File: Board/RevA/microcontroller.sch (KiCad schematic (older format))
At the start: 3 parts

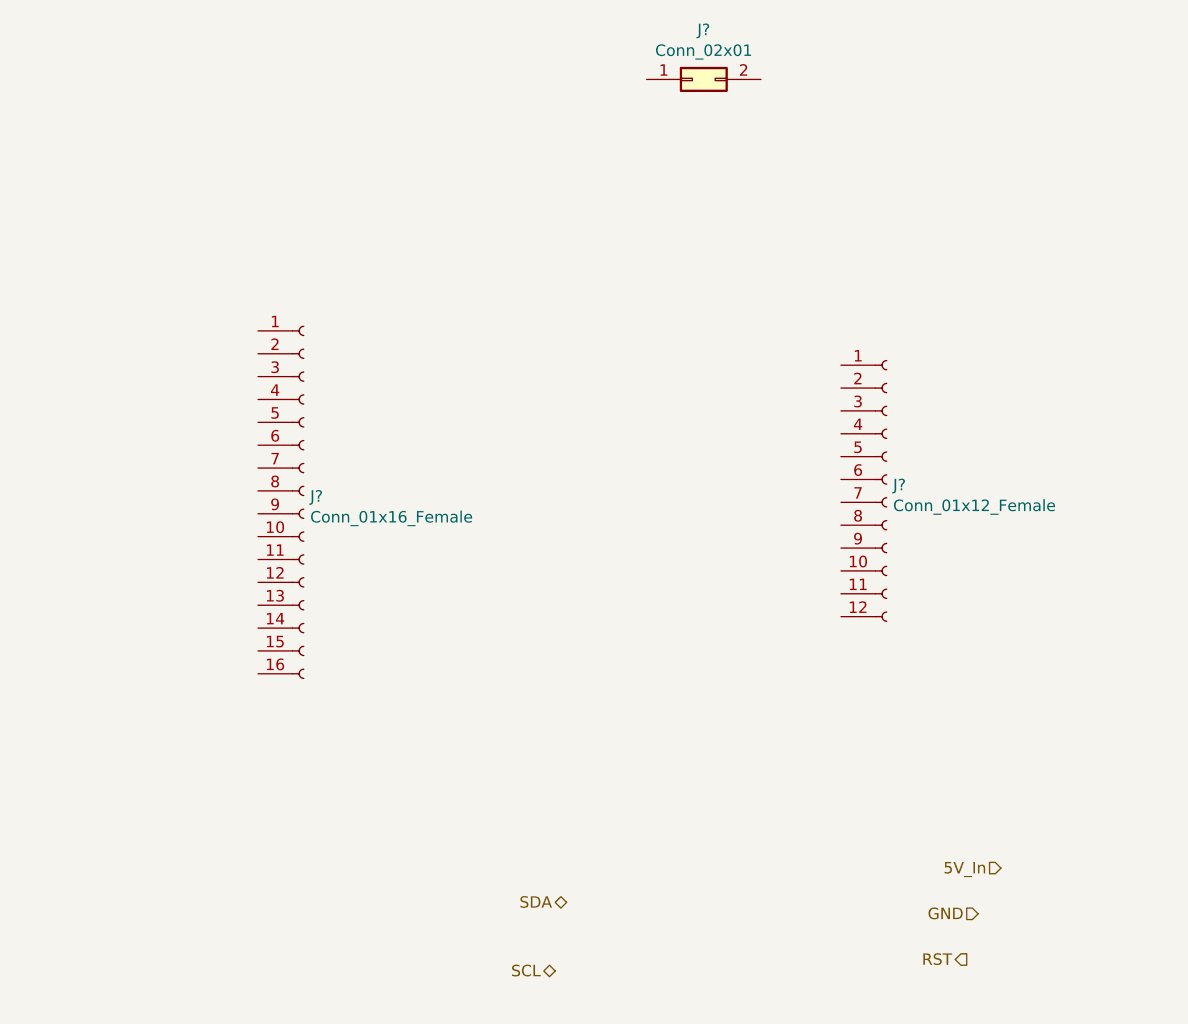
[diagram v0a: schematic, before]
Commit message: Added Microcontroller Logic to RevA
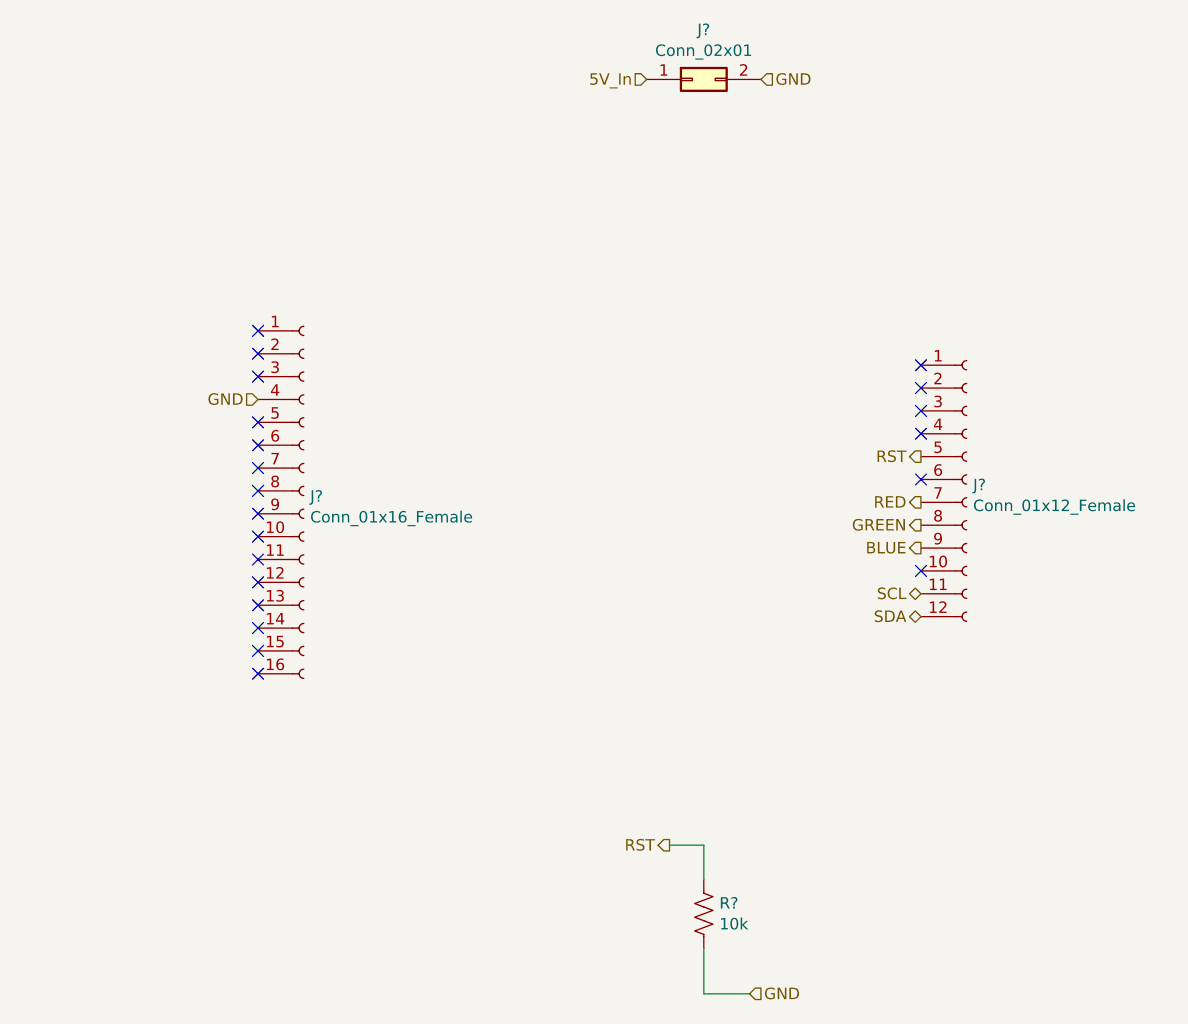
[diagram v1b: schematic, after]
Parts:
- added R?: 10k, symbol Device:R_US
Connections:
- net 5V_In: now also J?.1 (Pin_1)
- net GND: now also J?.2 (Pin_2), J?.4 (Pin_4), R?.2
- net RST: now also J?.5 (Pin_5), R?.1
- net SCL: now also J?.11 (Pin_11)
- net SDA: now also J?.12 (Pin_12)
- net RED: now reaches J?.7 (Pin_7)
- net GREEN: now reaches J?.8 (Pin_8)
- net BLUE: now reaches J?.9 (Pin_9)
- no-connect marks 0 -> 21
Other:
- moved on the sheet: J?
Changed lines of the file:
@@
 L Connector:Conn_01x12_Female J?
 U 1 1 614B7706
-P 6350 3300
+P 6700 3300
 AR Path="/614B7706" Ref="J?"  Part="1"
 AR Path="/614B5FF9/614B7706" Ref="J?"  Part="1"
-F 0 "J?" H 6378 3276 50  0000 L CNN
-F 1 "Conn_01x12_Female" H 6378 3185 50  0000 L CNN
-F 2 "" H 6350 3300 50  0001 C CNN
-F 3 "~" H 6350 3300 50  0001 C CNN
-	1    6350 3300
+F 0 "J?" H 6728 3276 50  0000 L CNN
+F 1 "Conn_01x12_Female" H 6728 3185 50  0000 L CNN
+F 2 "" H 6700 3300 50  0001 C CNN
+F 3 "~" H 6700 3300 50  0001 C CNN
+	1    6700 3300
 	1    0    0    -1
 $EndComp
-Text HLabel 4950 5150 0    50   BiDi ~ 0
+Text HLabel 6500 3900 0    50   BiDi ~ 0
 SDA
-Text HLabel 4900 5450 0    50   BiDi ~ 0
+Text HLabel 6500 3800 0    50   BiDi ~ 0
 SCL
 $Comp
@@
 	1    0    0    -1
 $EndComp
-Text HLabel 6850 5000 0    50   Input ~ 0
+Text HLabel 5300 1550 0    50   Input ~ 0
 5V_In
-Text HLabel 6750 5200 0    50   Input ~ 0
+Text HLabel 5800 1550 2    50   Input ~ 0
 GND
-Text HLabel 6700 5400 0    50   Output ~ 0
+Text HLabel 3600 2950 0    50   Input ~ 0
+GND
+Text HLabel 6500 3200 0    50   Output ~ 0
 RST
+Wire Wire Line
+	5550 4900 5550 5050
+Wire Wire Line
+	5400 4900 5550 4900
+Text HLabel 5400 4900 0    50   Output ~ 0
+RST
+$Comp
+L Device:R_US R?
+U 1 1 614ADABC
+P 5550 5200
+AR Path="/614ADABC" Ref="R?"  Part="1"
+AR Path="/614B5FF9/614ADABC" Ref="R?"  Part="1"
+F 0 "R?" H 5618 5246 50  0000 L CNN
+F 1 "10k" H 5618 5155 50  0000 L CNN
+F 2 "" V 5590 5190 50  0001 C CNN
+F 3 "~" H 5550 5200 50  0001 C CNN
+	1    5550 5200
+	1    0    0    -1
+$EndComp
+Text HLabel 5750 5550 2    50   Input ~ 0
+GND
+Wire Wire Line
+	5550 5350 5550 5550
+Wire Wire Line
+	5550 5550 5750 5550
+Text HLabel 6500 3400 0    50   Output ~ 0
+RED
+Text HLabel 6500 3500 0    50   Output ~ 0
+GREEN
+Text HLabel 6500 3600 0    50   Output ~ 0
+BLUE
+NoConn ~ 6500 3700
+NoConn ~ 6500 3300
+NoConn ~ 6500 3100
+NoConn ~ 6500 3000
+NoConn ~ 6500 2900
+NoConn ~ 6500 2800
+NoConn ~ 3600 4150
+NoConn ~ 3600 4050
+NoConn ~ 3600 3950
+NoConn ~ 3600 3850
+NoConn ~ 3600 3750
+NoConn ~ 3600 3650
+NoConn ~ 3600 3550
+NoConn ~ 3600 3450
+NoConn ~ 3600 3350
+NoConn ~ 3600 3250
+NoConn ~ 3600 3150
+NoConn ~ 3600 3050
+NoConn ~ 3600 2850
+NoConn ~ 3600 2750
+NoConn ~ 3600 2650
 $EndSCHEMATC

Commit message: Finished Rough RevA and Added Annotations
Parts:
- gave numbers to parts that had none: 4
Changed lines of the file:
@@
 P 3800 3350
 AR Path="/614B7700" Ref="J?"  Part="1"
-AR Path="/614B5FF9/614B7700" Ref="J?"  Part="1"
-F 0 "J?" H 3828 3326 50  0000 L CNN
+AR Path="/614B5FF9/614B7700" Ref="J3"  Part="1"
+F 0 "J3" H 3828 3326 50  0000 L CNN
 F 1 "Conn_01x16_Female" H 3828 3235 50  0000 L CNN
 F 2 "" H 3800 3350 50  0001 C CNN
@@
 P 6700 3300
 AR Path="/614B7706" Ref="J?"  Part="1"
-AR Path="/614B5FF9/614B7706" Ref="J?"  Part="1"
-F 0 "J?" H 6728 3276 50  0000 L CNN
+AR Path="/614B5FF9/614B7706" Ref="J5"  Part="1"
+F 0 "J5" H 6728 3276 50  0000 L CNN
 F 1 "Conn_01x12_Female" H 6728 3185 50  0000 L CNN
 F 2 "" H 6700 3300 50  0001 C CNN
@@
 SCL
 $Comp
-L Connector_Generic:Conn_02x01 J?
+L Connector_Generic:Conn_02x01 J4
 U 1 1 614BCCF6
 P 5500 1550
-F 0 "J?" H 5550 1767 50  0000 C CNN
+F 0 "J4" H 5550 1767 50  0000 C CNN
 F 1 "Conn_02x01" H 5550 1676 50  0000 C CNN
 F 2 "" H 5500 1550 50  0001 C CNN
@@
 P 5550 5200
 AR Path="/614ADABC" Ref="R?"  Part="1"
-AR Path="/614B5FF9/614ADABC" Ref="R?"  Part="1"
-F 0 "R?" H 5618 5246 50  0000 L CNN
+AR Path="/614B5FF9/614ADABC" Ref="R7"  Part="1"
+F 0 "R7" H 5618 5246 50  0000 L CNN
 F 1 "10k" H 5618 5155 50  0000 L CNN
 F 2 "" V 5590 5190 50  0001 C CNN

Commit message: Added Footprints to RevA 1/2
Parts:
- R7: footprint (none) -> Resistor_SMD:R_0603_1608Metric
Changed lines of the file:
@@
 F 0 "R7" H 5618 5246 50  0000 L CNN
 F 1 "10k" H 5618 5155 50  0000 L CNN
-F 2 "" V 5590 5190 50  0001 C CNN
+F 2 "Resistor_SMD:R_0603_1608Metric" V 5590 5190 50  0001 C CNN
 F 3 "~" H 5550 5200 50  0001 C CNN
 	1    5550 5200

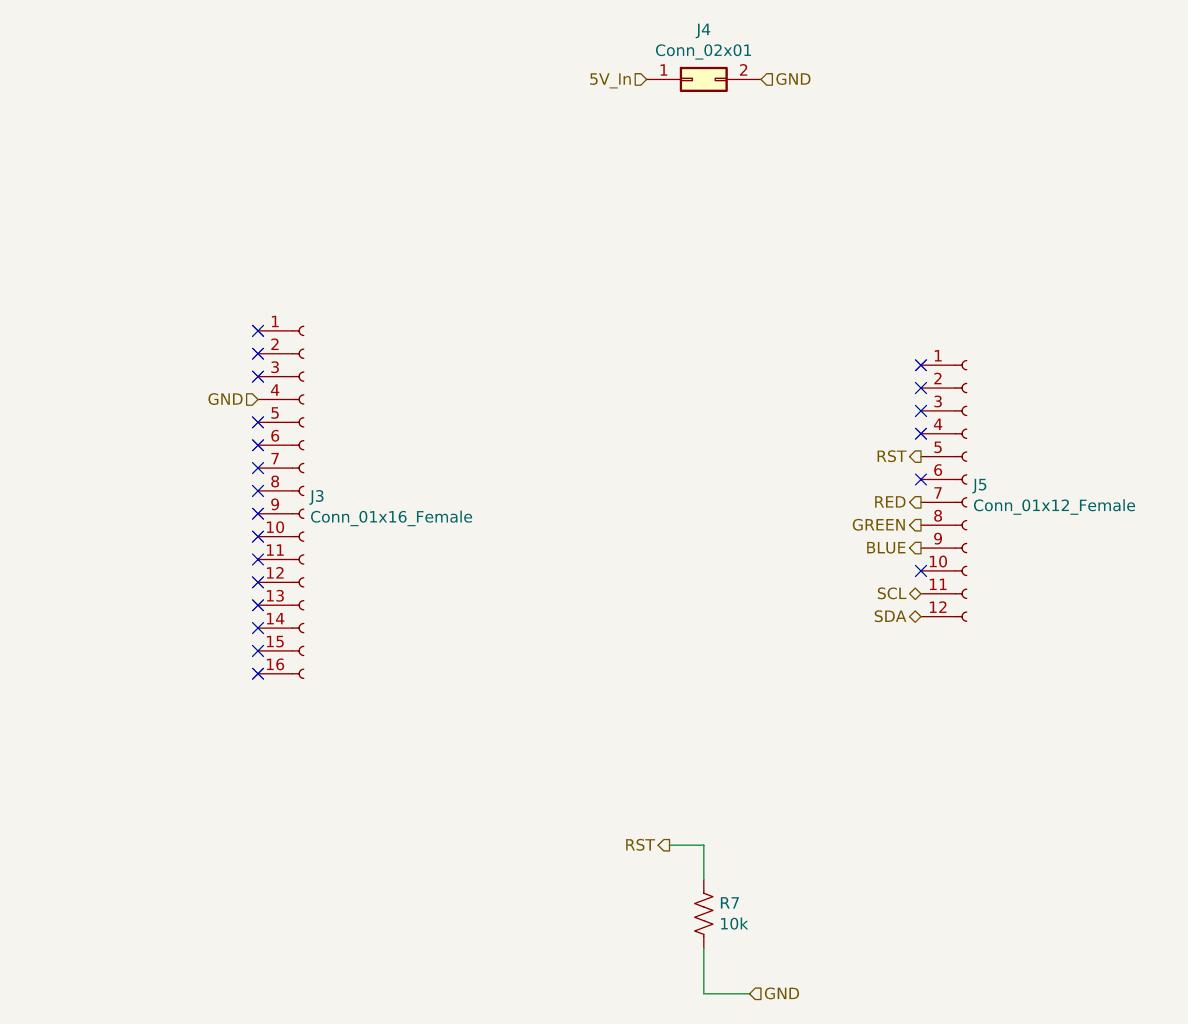
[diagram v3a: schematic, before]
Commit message: Updated Power Pins and Header Layout
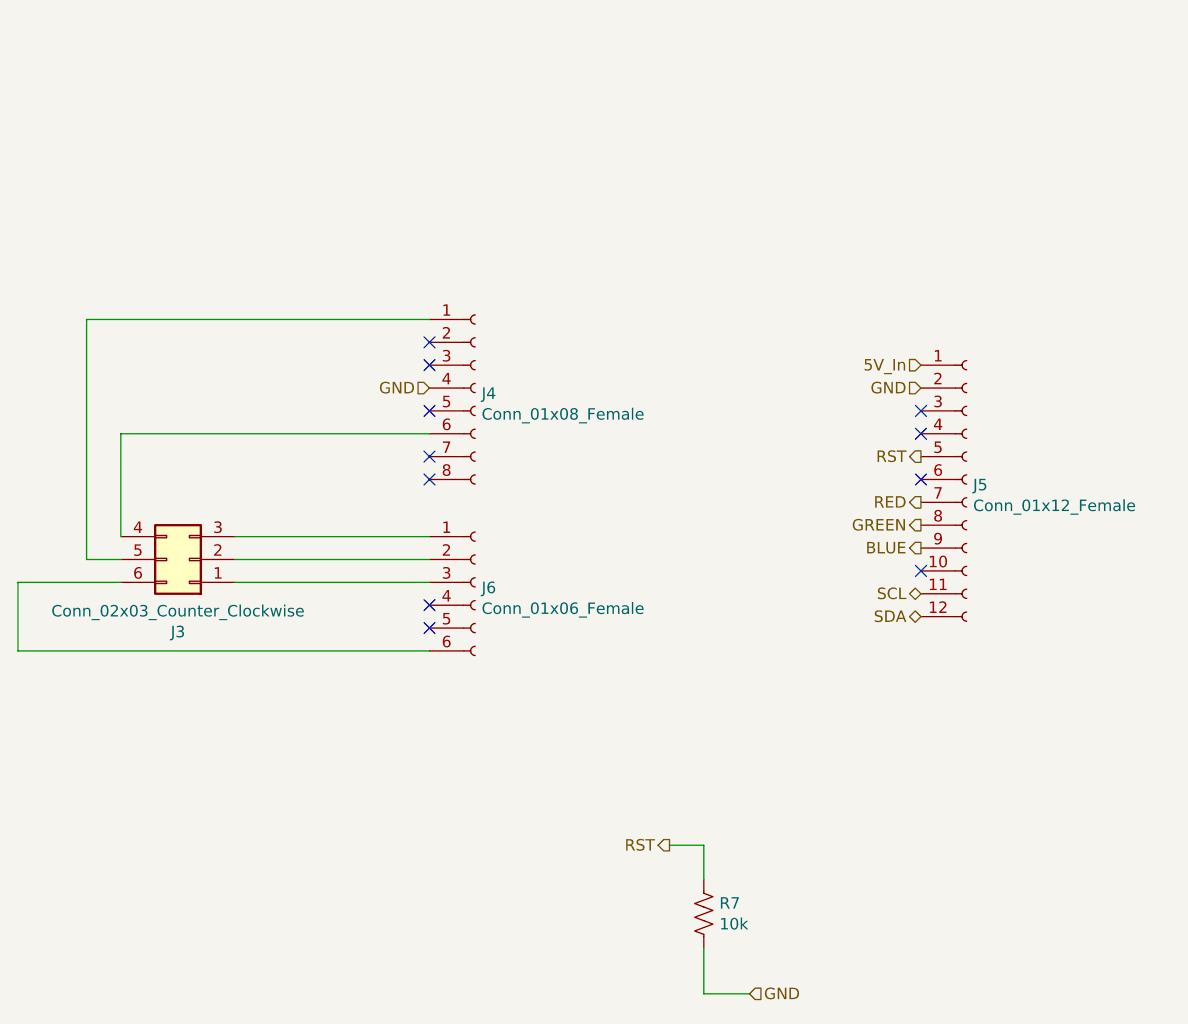
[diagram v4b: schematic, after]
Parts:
- removed J3: Conn_01x16_Female, symbol Connector:Conn_01x16_Female
- removed J4: Conn_02x01, symbol Connector_Generic:Conn_02x01
- added J3: Conn_02x03_Counter_Clockwise, Connector_PinHeader_2.54mm:PinHeader_2x03_P2.54mm_Vertical, symbol Connector_Generic:Conn_02x03_Counter_Clockwise
- added J4: Conn_01x08_Female, symbol Connector:Conn_01x08_Female
- added J6: Conn_01x06_Female, symbol Connector:Conn_01x06_Female
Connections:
- net 5V_In: now also J5.1 (Pin_1)
- net GND: now also J5.2 (Pin_2), J4.4 (Pin_4)
- new net: J3.5 (Pin_5), J4.1 (Pin_1)
- new net: J3.4 (Pin_4), J4.6 (Pin_6)
- new net: J3.3 (Pin_3), J6.1 (Pin_1)
- new net: J3.2 (Pin_2), J6.2 (Pin_2)
- new net: J3.1 (Pin_1), J6.3 (Pin_3)
- new net: J3.6 (Pin_6), J6.6 (Pin_6)
- no-connect marks 21 -> 11
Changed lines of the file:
@@
 $EndDescr
-$Comp
-L Connector:Conn_01x16_Female J?
-U 1 1 614B7700
-P 3800 3350
-AR Path="/614B7700" Ref="J?"  Part="1"
-AR Path="/614B5FF9/614B7700" Ref="J3"  Part="1"
-F 0 "J3" H 3828 3326 50  0000 L CNN
-F 1 "Conn_01x16_Female" H 3828 3235 50  0000 L CNN
-F 2 "" H 3800 3350 50  0001 C CNN
-F 3 "~" H 3800 3350 50  0001 C CNN
-	1    3800 3350
-	1    0    0    -1
-$EndComp
 $Comp
 L Connector:Conn_01x12_Female J?
@@
 Text HLabel 6500 3800 0    50   BiDi ~ 0
 SCL
-$Comp
-L Connector_Generic:Conn_02x01 J4
-U 1 1 614BCCF6
-P 5500 1550
-F 0 "J4" H 5550 1767 50  0000 C CNN
-F 1 "Conn_02x01" H 5550 1676 50  0000 C CNN
-F 2 "" H 5500 1550 50  0001 C CNN
-F 3 "~" H 5500 1550 50  0001 C CNN
-	1    5500 1550
-	1    0    0    -1
-$EndComp
-Text HLabel 5300 1550 0    50   Input ~ 0
+Text HLabel 6500 2800 0    50   Input ~ 0
 5V_In
-Text HLabel 5800 1550 2    50   Input ~ 0
+Text HLabel 6500 2900 0    50   Input ~ 0
 GND
-Text HLabel 3600 2950 0    50   Input ~ 0
+Text HLabel 4350 2900 0    50   Input ~ 0
 GND
 Text HLabel 6500 3200 0    50   Output ~ 0
@@
 NoConn ~ 6500 3100
 NoConn ~ 6500 3000
-NoConn ~ 6500 2900
-NoConn ~ 6500 2800
-NoConn ~ 3600 4150
-NoConn ~ 3600 4050
-NoConn ~ 3600 3950
-NoConn ~ 3600 3850
-NoConn ~ 3600 3750
-NoConn ~ 3600 3650
-NoConn ~ 3600 3550
-NoConn ~ 3600 3450
-NoConn ~ 3600 3350
-NoConn ~ 3600 3250
-NoConn ~ 3600 3150
-NoConn ~ 3600 3050
-NoConn ~ 3600 2850
-NoConn ~ 3600 2750
-NoConn ~ 3600 2650
+NoConn ~ 4350 3950
+NoConn ~ 4350 3850
+NoConn ~ 4350 3300
+NoConn ~ 4350 3200
+NoConn ~ 4350 3000
+NoConn ~ 4350 2800
+NoConn ~ 4350 2700
+$Comp
+L Connector:Conn_01x08_Female J4
+U 1 1 615111EC
+P 4550 2900
+F 0 "J4" H 4578 2876 50  0000 L CNN
+F 1 "Conn_01x08_Female" H 4578 2785 50  0000 L CNN
+F 2 "" H 4550 2900 50  0001 C CNN
+F 3 "~" H 4550 2900 50  0001 C CNN
+	1    4550 2900
+	1    0    0    -1
+$EndComp
+$Comp
+L Connector:Conn_01x06_Female J6
+U 1 1 61514301
+P 4550 3750
+F 0 "J6" H 4578 3726 50  0000 L CNN
+F 1 "Conn_01x06_Female" H 4578 3635 50  0000 L CNN
+F 2 "" H 4550 3750 50  0001 C CNN
+F 3 "~" H 4550 3750 50  0001 C CNN
+	1    4550 3750
+	1    0    0    -1
+$EndComp
+$Comp
+L Connector_Generic:Conn_02x03_Counter_Clockwise J3
+U 1 1 6151B2EA
+P 3300 3650
+F 0 "J3" H 3350 3967 50  0000 C CNN
+F 1 "Conn_02x03_Counter_Clockwise" H 3350 3876 50  0000 C CNN
+F 2 "Connector_PinHeader_2.54mm:PinHeader_2x03_P2.54mm_Vertical" H 3300 3650 50  0001 C CNN
+F 3 "~" H 3300 3650 50  0001 C CNN
+	1    3300 3650
+	-1   0    0    1
+$EndComp
+Wire Wire Line
+	4350 3550 3500 3550
+Wire Wire Line
+	4350 3650 3500 3650
+Wire Wire Line
+	4350 3750 3500 3750
+Wire Wire Line
+	4350 4050 2550 4050
+Wire Wire Line
+	2550 4050 2550 3750
+Wire Wire Line
+	2550 3750 3000 3750
+Wire Wire Line
+	4350 3100 3000 3100
+Wire Wire Line
+	3000 3100 3000 3550
+Wire Wire Line
+	3000 3650 2850 3650
+Wire Wire Line
+	2850 3650 2850 2600
+Wire Wire Line
+	2850 2600 4350 2600
 $EndSCHEMATC

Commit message: Created Female Pin Header Footprints
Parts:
- J4: footprint (none) -> 0_MSD_FPs:MSD_8_Pin
- J5: footprint (none) -> 0_MSD_FPs:MSD_12_Pin
- J6: footprint (none) -> 0_MSD_FPs:MSD_6_Pin
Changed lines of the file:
@@
 F 0 "J5" H 6728 3276 50  0000 L CNN
 F 1 "Conn_01x12_Female" H 6728 3185 50  0000 L CNN
-F 2 "" H 6700 3300 50  0001 C CNN
+F 2 "0_MSD_FPs:MSD_12_Pin" H 6700 3300 50  0001 C CNN
 F 3 "~" H 6700 3300 50  0001 C CNN
 	1    6700 3300
@@
 F 0 "J4" H 4578 2876 50  0000 L CNN
 F 1 "Conn_01x08_Female" H 4578 2785 50  0000 L CNN
-F 2 "" H 4550 2900 50  0001 C CNN
+F 2 "0_MSD_FPs:MSD_8_Pin" H 4550 2900 50  0001 C CNN
 F 3 "~" H 4550 2900 50  0001 C CNN
 	1    4550 2900
@@
 F 0 "J6" H 4578 3726 50  0000 L CNN
 F 1 "Conn_01x06_Female" H 4578 3635 50  0000 L CNN
-F 2 "" H 4550 3750 50  0001 C CNN
+F 2 "0_MSD_FPs:MSD_6_Pin" H 4550 3750 50  0001 C CNN
 F 3 "~" H 4550 3750 50  0001 C CNN
 	1    4550 3750
